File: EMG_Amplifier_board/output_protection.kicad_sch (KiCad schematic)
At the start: 2 parts

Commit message: add footprints
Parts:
- D3: footprint (none) -> Diode_SMD:D_SOD-523
- R5: value 330 -> 330R; footprint (none) -> Resistor_SMD:R_0805_2012Metric
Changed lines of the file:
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@@
+		)
+	)
+	(hierarchical_label "GND"
+		(shape input)
+		(at 124.46 111.76 270)
+		(fields_autoplaced yes)
+		(effects
+			(font
+				(size 1.27 1.27)
+			)
+			(justify right)
 		)
 	)
@@
 	)
 	(symbol
-		(lib_id "power:GND")
-		(at 124.46 111.76 0)
-		(unit 1)
-		(exclude_from_sim no)
-		(in_bom yes)
-		(on_board yes)
-		(dnp no)
-		(fields_autoplaced yes)
-		(property "Reference" "#PWR01"
-			(at 124.46 118.11 0)
-			(effects
-				(font
-					(size 1.27 1.27)
-				)
-				(hide yes)
-			)
-		)
-		(property "Value" "GND"
-			(at 124.46 116.84 0)
-			(effects
-				(font
-					(size 1.27 1.27)
-				)
-			)
-		)
-		(property "Footprint" ""
-			(at 124.46 111.76 0)
-			(effects
-				(font
-					(size 1.27 1.27)
-				)
-				(hide yes)
-			)
-		)
-		(property "Datasheet" ""
-			(at 124.46 111.76 0)
-			(effects
-				(font
-					(size 1.27 1.27)
-				)
-				(hide yes)
-			)
-		)
-		(property "Description" "Power symbol creates a global label with name \"GND\" , ground"
-			(at 124.46 111.76 0)
-			(effects
-				(font
-					(size 1.27 1.27)
-				)
-				(hide yes)
-			)
-		)
-		(pin "1"
-		)
-		(instances
-			(project ""
-				(path "/26861adc-1ddf-4c37-9f8b-8db1c0839771/116d6144-bb2d-4875-b0ee-35e8a6acfcf1"
-					(reference "#PWR01")
-					(unit 1)
-				)
-			)
-		)
-	)
-	(symbol
 		(lib_id "Device:R")
 		(at 114.3 105.41 90)
@@
 			)
 		)
-		(property "Value" "330"
+		(property "Value" "330R"
 			(at 114.3 101.6 90)
 			(effects
@@
 			)
 		)
-		(property "Footprint" ""
+		(property "Footprint" "Resistor_SMD:R_0805_2012Metric"
 			(at 114.3 107.188 90)
 			(effects
@@
 			)
 		)
-		(property "Footprint" ""
+		(property "Footprint" "Diode_SMD:D_SOD-523"
 			(at 135.89 105.41 0)
 			(effects

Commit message: acomponents choice
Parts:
- R5: footprint Resistor_SMD:R_0805_2012Metric -> Resistor_SMD:R_0402_1005Metric
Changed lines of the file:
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@@
 			)
 		)
-		(property "Footprint" "Resistor_SMD:R_0805_2012Metric"
+		(property "Footprint" "Resistor_SMD:R_0402_1005Metric"
 			(at 114.3 107.188 90)
 			(effects

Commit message: pcb design v1
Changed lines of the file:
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@@
-		)
-	)
-	(hierarchical_label "GND"
-		(shape input)
-		(at 124.46 111.76 270)
-		(fields_autoplaced yes)
-		(effects
-			(font
-				(size 1.27 1.27)
-			)
-			(justify right)
 		)
 	)
@@
 					(unit 1)
 				)
+			)
+		)
+	)
+	(symbol
+		(lib_id "power:GND")
+		(at 124.46 111.76 0)
+		(unit 1)
+		(exclude_from_sim no)
+		(in_bom yes)
+		(on_board yes)
+		(dnp no)
+		(fields_autoplaced yes)
+		(property "Reference" "#PWR01"
+			(at 124.46 118.11 0)
+			(effects
+				(font
+					(size 1.27 1.27)
+				)
+				(hide yes)
+			)
+		)
+		(property "Value" "GND"
+			(at 124.46 116.84 0)
+			(effects
+				(font
+					(size 1.27 1.27)
+				)
+			)
+		)
+		(property "Footprint" ""
+			(at 124.46 111.76 0)
+			(effects
+				(font
+					(size 1.27 1.27)
+				)
+				(hide yes)
+			)
+		)
+		(property "Datasheet" ""
+			(at 124.46 111.76 0)
+			(effects
+				(font
+					(size 1.27 1.27)
+				)
+				(hide yes)
+			)
+		)
+		(property "Description" "Power symbol creates a global label with name \"GND\" , ground"
+			(at 124.46 111.76 0)
+			(effects
+				(font
+					(size 1.27 1.27)
+				)
+				(hide yes)
+			)
+		)
+		(pin "1"
+		)
+		(instances
+			(project ""
+				(path "/26861adc-1ddf-4c37-9f8b-8db1c0839771/5ea975e8-3227-4877-bc8b-ac5d6b7605f1/f0ef1686-4824-423f-8bc9-279e47f6fa27"
+					(reference "#PWR01")
+					(unit 1)
+				)

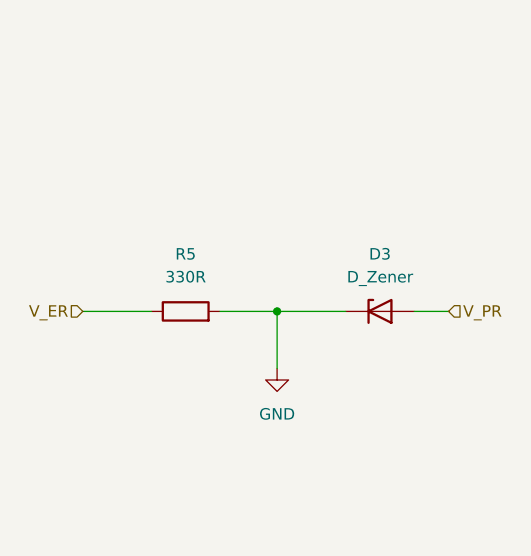
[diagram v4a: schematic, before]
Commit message: center the pin connectors
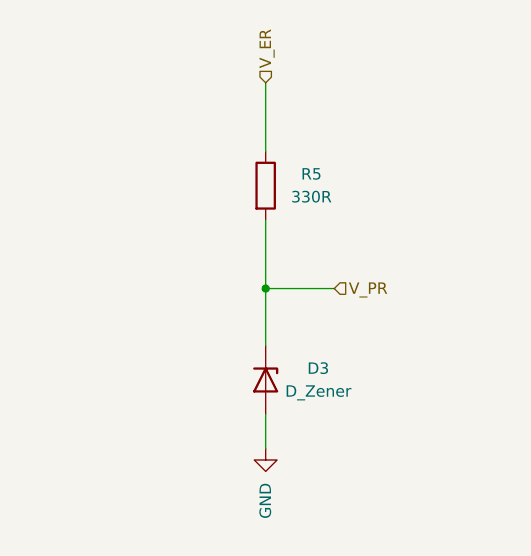
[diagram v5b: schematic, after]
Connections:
- net GND: now also D3.2 (A); no longer D3.1 (K), R5.2
- net V_PR: now also D3.1 (K), R5.2; no longer D3.2 (A)
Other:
- moved on the sheet: D3, R5
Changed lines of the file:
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@@
 	(paper "A4")
 	(junction
-		(at 124.46 105.41)
+		(at 123.19 102.87)
 		(diameter 0)
 		(color 0 0 0 0)
@@
 	(wire
 		(pts
-			(xy 118.11 105.41) (xy 124.46 105.41)
-		)
-		(stroke
-			(width 0)
-			(type default)
-		)
-	)
-	(wire
-		(pts
-			(xy 139.7 105.41) (xy 143.51 105.41)
-		)
-		(stroke
-			(width 0)
-			(type default)
-		)
-	)
-	(wire
-		(pts
-			(xy 124.46 105.41) (xy 124.46 111.76)
-		)
-		(stroke
-			(width 0)
-			(type default)
-		)
-	)
-	(wire
-		(pts
-			(xy 132.08 105.41) (xy 124.46 105.41)
-		)
-		(stroke
-			(width 0)
-			(type default)
-		)
-	)
-	(wire
-		(pts
-			(xy 102.87 105.41) (xy 110.49 105.41)
+			(xy 123.19 95.25) (xy 123.19 102.87)
+		)
+		(stroke
+			(width 0)
+			(type default)
+		)
+	)
+	(wire
+		(pts
+			(xy 123.19 116.84) (xy 123.19 120.65)
+		)
+		(stroke
+			(width 0)
+			(type default)
+		)
+	)
+	(wire
+		(pts
+			(xy 130.81 102.87) (xy 123.19 102.87)
+		)
+		(stroke
+			(width 0)
+			(type default)
+		)
+	)
+	(wire
+		(pts
+			(xy 123.19 102.87) (xy 123.19 109.22)
+		)
+		(stroke
+			(width 0)
+			(type default)
+		)
+	)
+	(wire
+		(pts
+			(xy 123.19 80.01) (xy 123.19 87.63)
 		)
 		(stroke
@@
 	(hierarchical_label "V_ER"
 		(shape input)
-		(at 102.87 105.41 180)
+		(at 123.19 80.01 90)
 		(fields_autoplaced yes)
 		(effects
@@
 				(size 1.27 1.27)
 			)
-			(justify right)
+			(justify left)
 		)
 	)
 	(hierarchical_label "V_PR"
 		(shape input)
-		(at 143.51 105.41 0)
+		(at 130.81 102.87 0)
 		(fields_autoplaced yes)
 		(effects
@@
 	(symbol
 		(lib_id "Device:R")
-		(at 114.3 105.41 90)
+		(at 123.19 91.44 0)
 		(unit 1)
 		(exclude_from_sim no)
@@
 		(on_board yes)
 		(dnp no)
-		(fields_autoplaced yes)
 		(property "Reference" "R5"
-			(at 114.3 99.06 90)
+			(at 128.27 90.17 0)
 			(effects
 				(font
@@
 		)
 		(property "Value" "330R"
-			(at 114.3 101.6 90)
+			(at 128.27 92.71 0)
 			(effects
 				(font
@@
 		)
 		(property "Footprint" "Resistor_SMD:R_0402_1005Metric"
-			(at 114.3 107.188 90)
+			(at 121.412 91.44 90)
 			(effects
 				(font
@@
 		)
 		(property "Datasheet" "~"
-			(at 114.3 105.41 0)
+			(at 123.19 91.44 0)
 			(effects
 				(font
@@
 		)
 		(property "Description" "Resistor"
-			(at 114.3 105.41 0)
+			(at 123.19 91.44 0)
 			(effects
 				(font
@@
 	(symbol
 		(lib_id "Device:D_Zener")
-		(at 135.89 105.41 0)
+		(at 123.19 113.03 270)
 		(unit 1)
 		(exclude_from_sim no)
@@
 		(on_board yes)
 		(dnp no)
-		(fields_autoplaced yes)
 		(property "Reference" "D3"
-			(at 135.89 99.06 0)
+			(at 129.032 111.76 90)
 			(effects
 				(font
@@
 		)
 		(property "Value" "D_Zener"
-			(at 135.89 101.6 0)
+			(at 129.032 114.3 90)
 			(effects
 				(font
@@
 		)
 		(property "Footprint" "Diode_SMD:D_SOD-523"
-			(at 135.89 105.41 0)
+			(at 123.19 113.03 0)
 			(effects
 				(font
@@
 		)
 		(property "Datasheet" "~"
-			(at 135.89 105.41 0)
+			(at 123.19 113.03 0)
 			(effects
 				(font
@@
 		)
 		(property "Description" "Zener diode"
-			(at 135.89 105.41 0)
+			(at 123.19 113.03 0)
 			(effects
 				(font
@@
 	(symbol
 		(lib_id "power:GND")
-		(at 124.46 111.76 0)
+		(at 123.19 120.65 0)
 		(unit 1)
 		(exclude_from_sim no)
@@
 		(fields_autoplaced yes)
 		(property "Reference" "#PWR01"
-			(at 124.46 118.11 0)
+			(at 123.19 127 0)
 			(effects
 				(font
@@
 		)
 		(property "Value" "GND"
-			(at 124.46 116.84 0)
-			(effects
-				(font
-					(size 1.27 1.27)
-				)
+			(at 123.1901 124.46 90)
+			(effects
+				(font
+					(size 1.27 1.27)
+				)
+				(justify right)
 			)
 		)
 		(property "Footprint" ""
-			(at 124.46 111.76 0)
+			(at 123.19 120.65 0)
 			(effects
 				(font
@@
 		)
 		(property "Datasheet" ""
-			(at 124.46 111.76 0)
+			(at 123.19 120.65 0)
 			(effects
 				(font
@@
 		)
 		(property "Description" "Power symbol creates a global label with name \"GND\" , ground"
-			(at 124.46 111.76 0)
-			(effects
-				(font
+			(at 123.19 120.65 0)
+			(effects
+				(font

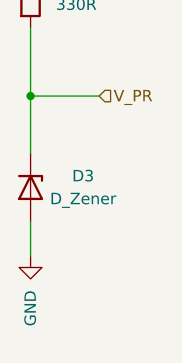
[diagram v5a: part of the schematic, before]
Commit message: remove panel design
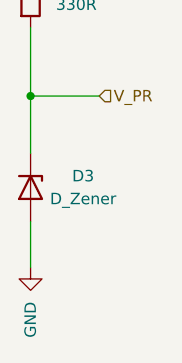
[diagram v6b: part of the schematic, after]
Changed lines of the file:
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@@
+	(wire
+		(pts
+			(xy 123.19 116.84) (xy 123.19 121.92)
+		)
+		(stroke
+			(width 0)
+			(type default)
+		)
+	)
 	(wire
 		(pts
 			(xy 123.19 95.25) (xy 123.19 102.87)
-		)
-		(stroke
-			(width 0)
-			(type default)
-		)
-	)
-	(wire
-		(pts
-			(xy 123.19 116.84) (xy 123.19 120.65)
 		)
 		(stroke
@@
 	(symbol
 		(lib_id "power:GND")
-		(at 123.19 120.65 0)
+		(at 123.19 121.92 0)
 		(unit 1)
 		(exclude_from_sim no)
@@
 		(fields_autoplaced yes)
 		(property "Reference" "#PWR01"
-			(at 123.19 127 0)
+			(at 123.19 128.27 0)
 			(effects
 				(font
@@
 		)
 		(property "Value" "GND"
-			(at 123.1901 124.46 90)
+			(at 123.1901 125.73 90)
 			(effects
 				(font
@@
 		)
 		(property "Footprint" ""
-			(at 123.19 120.65 0)
+			(at 123.19 121.92 0)
 			(effects
 				(font
@@
 		)
 		(property "Datasheet" ""
-			(at 123.19 120.65 0)
+			(at 123.19 121.92 0)
 			(effects
 				(font
@@
 		)
 		(property "Description" "Power symbol creates a global label with name \"GND\" , ground"
-			(at 123.19 120.65 0)
-			(effects
-				(font
+			(at 123.19 121.92 0)
+			(effects
+				(font
